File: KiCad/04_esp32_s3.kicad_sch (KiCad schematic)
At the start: 28 parts, among them IC101 ESP32-S3-WROOM-1-N16R8, Q300 SS8050, Q301 SS8050

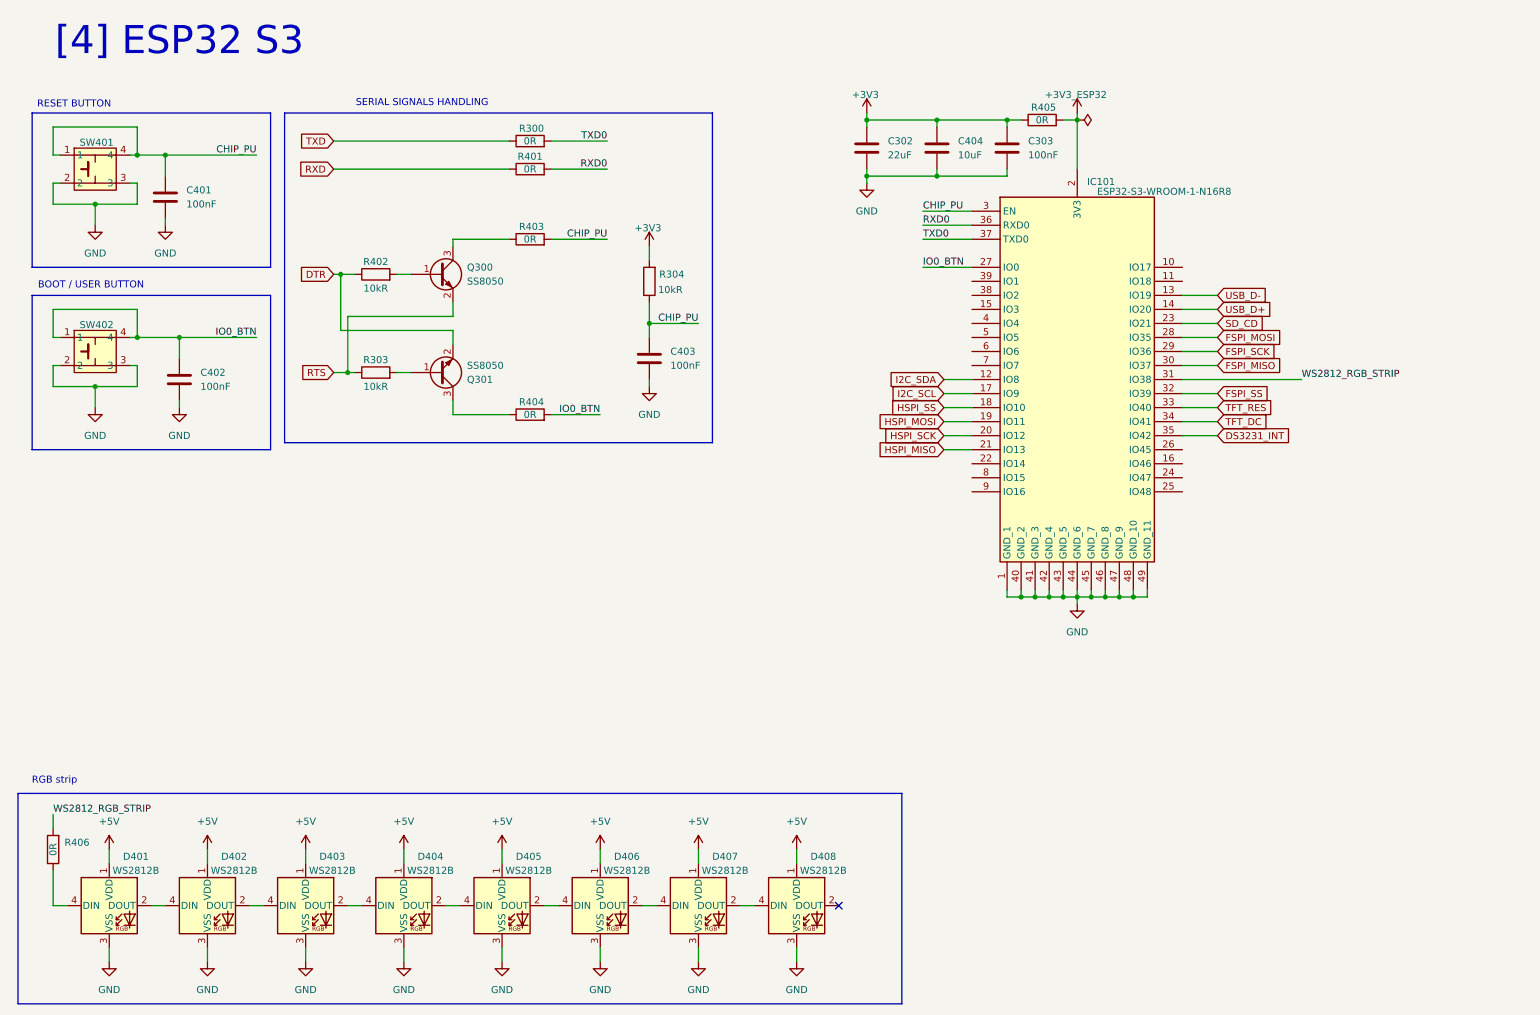
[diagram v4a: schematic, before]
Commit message: Add analog sensors
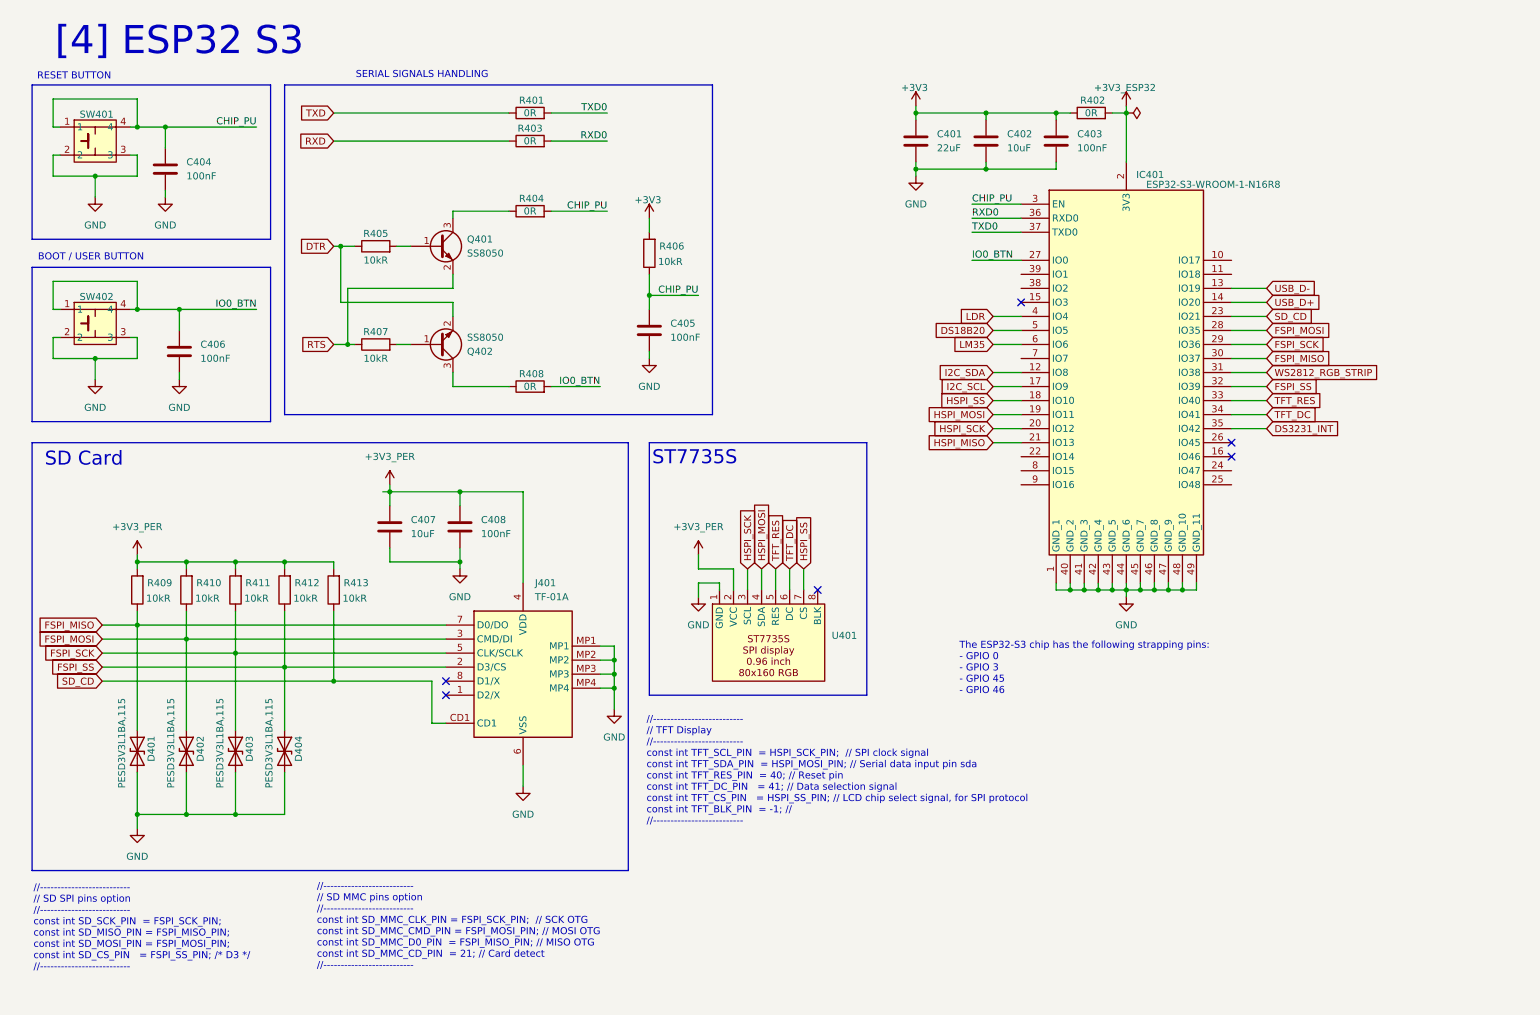
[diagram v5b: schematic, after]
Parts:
- removed D401, D402, D403, D404, D405, D406, D407, D408: WS2812B, LED_SMD:LED_WS2812B_PLCC4_5.0x5.0mm_P3.2mm, symbol LED:WS2812B
- removed R406: 0R, Resistor_SMD:R_0805_2012Metric, symbol Device:R
- added C407: 10uF, Capacitor_SMD:C_0603_1608Metric, symbol Device:C
- added C408: 100nF, Capacitor_SMD:C_0603_1608Metric, symbol Device:C
- added D401, D402, D403, D404: PESD3V3L1BA,115, Diode_SMD:D_SOD-323, symbol Device:D_TVS
- added J401: TF-01A, esp32_s3_weather_webserver:TF01A, symbol esp32_s3_weather_webserver:TF-01A
- added R409, R410, R411, R412, R413: 10kR, Resistor_SMD:R_0805_2012Metric, symbol Device:R
- added U401: ~, symbol esp32_s3_weather_webserver:ST7735S
- renumbered C302 to C401, C404 to C402, C303 to C403, C401 to C404, C403 to C405, C402 to C406, IC101 to IC401, Q300 to Q401, Q301 to Q402, R300 to R401, R405 to R402, R401 to R403, R403 to R404, R402 to R405, R304 to R406, R303 to R407, R404 to R408
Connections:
- net FSPI_MISO: now also D401.1 (A1), J401.7 (D0/DO), R409.1
- net FSPI_MOSI: now also D402.1 (A1), J401.3 (CMD/DI), R410.1
- net FSPI_SCK: now also D403.1 (A1), J401.5 (CLK/SCLK), R411.1
- net FSPI_SS: now also D404.1 (A1), J401.2 (D3/CS), R412.1
- net GND: now also C407.2, C408.2, D401.2 (A2), D402.2 (A2), D403.2 (A2), D404.2 (A2), J401.6 (VSS), J401.MP1, J401.MP2, J401.MP3, J401.MP4, U401.1 (GND)
- net HSPI_MOSI: now also U401.4 (SDA)
- net HSPI_SCK: now also U401.3 (SCL)
- net HSPI_SS: now also U401.7 (CS)
- net SD_CD: now also J401.CD1, R413.1
- net TFT_DC: now also U401.6 (DC)
- net TFT_RES: now also U401.5 (RES)
- net LDR: now reaches IC401.4 (IO4)
- net DS18B20: now reaches IC401.5 (IO5)
- net LM35: now reaches IC401.6 (IO6)
- new net +3V3_PER: C407.1, C408.1, J401.4 (VDD), R409.2, R410.2, R411.2, R412.2, R413.2, U401.2 (VCC)
- no-connect marks 1 -> 6
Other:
- note added: "//-------------------------- // SD MMC pins option //-------------------------- const int SD_MMC_CLK_PIN = FSPI_SCK_PIN; // SCK OTG const int SD_MMC_CMD_PIN = FSPI_MOSI_PIN; // MOSI OTG const int SD_MMC_D0_PIN = FSPI_MISO_PIN; // MISO OTG const int SD_MMC_CD_PIN = 21; // Card detect //--------------------------"
- note added: "//-------------------------- // SD SPI pins option //-------------------------- const int SD_SCK_PIN = FSPI_SCK_PIN; const int SD_MISO_PIN = FSPI_MISO_PIN; const int SD_MOSI_PIN = FSPI_MOSI_PIN; const int SD_CS_PIN = FSPI_SS_PIN; /* D3 */ //--------------------------"
- note added: "//-------------------------- // TFT Display //-------------------------- const int TFT_SCL_PIN = HSPI_SCK_PIN; // SPI clock signal const int TFT_SDA_PIN = HSPI_MOSI_PIN; // Serial data input pin sda const int TFT_RES_PIN = 40; // Reset pin const int TFT_DC_PIN = 41; // Data selection signal const int TFT_CS_PIN = HSPI_SS_PIN; // LCD chip select signal, for SPI protocol const int TFT_BLK_PIN = -1;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"
- note added: "SD Card"
- note added: "ST7735S"
- note added: "The ESP32-S3 chip has the following strapping pins: - GPIO 0 - GPIO 3 - GPIO 45 - GPIO 46"
- note removed: "RGB strip"
- moved on the sheet: C401, C402, C403, C404, C405, C406, IC401, Q401, Q402, R401, R402, R403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

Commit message: First scheme version
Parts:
- added C409: 100nF, Capacitor_SMD:C_0603_1608Metric, symbol Device:C
- added J401, J403: Conn_01x04_Pin, Connector_PinHeader_2.54mm:PinHeader_1x04_P2.54mm_Vertical, symbol Connector:Conn_01x04_Pin
- added J402: Conn_01x12_Pin, Connector_PinHeader_2.54mm:PinHeader_1x12_P2.54mm_Vertical, symbol Connector:Conn_01x12_Pin
- added R409: 10kR, Resistor_SMD:R_0805_2012Metric, symbol Device:R
- added SW403: ~, esp32_s3_weather_webserver:SW_PUSH_6mm_H5mm, symbol esp32_s3_weather_webserver:SW_PUSH_6mm_H5mm
- Q401, Q402: Manufacturer Jiangsu Changjing Electronics Technology Co., Ltd. -> (none); Manufacturer Part Number SS8050(RANGE:200-350) -> (none)
- renumbered J401 to J404, R402 to R401, R401 to R402, R406 to R404, R404 to R405, R405 to R406, R409 to R410, R410 to R411, R411 to R412, R412 to R413, R413 to R414
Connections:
- net +3V3: now also R409.1
- net +3V3_PER: now also J401.2 (Pin_2), J402.2 (Pin_2), J403.2 (Pin_2)
- net GND: now also C409.2, J401.1 (Pin_1), J402.10 (Pin_10), J402.4 (Pin_4), J402.6 (Pin_6), J403.1 (Pin_1), SW403.2, SW403.3
- net I2C_SCL: now also J403.4 (Pin_4)
- net I2C_SDA: now also J403.3 (Pin_3)
- net GPIO17: now reaches IC401.10 (IO17)
- net GPIO17: now also J402.8 (Pin_8)
- net GPIO18: now reaches IC401.11 (IO18)
- net GPIO18: now also J402.9 (Pin_9)
- net GPIO14: now reaches IC401.22 (IO14)
- net GPIO14: now also J402.7 (Pin_7)
- net GPIO47: now reaches IC401.24 (IO47)
- net GPIO47: now also J402.11 (Pin_11)
- net GPIO48: now reaches IC401.25 (IO48)
- net GPIO48: now also J402.12 (Pin_12)
- net GPIO2: now reaches IC401.38 (IO2)
- net GPIO2: now also J402.5 (Pin_5)
- net USR_BTN: now reaches IC401.39 (IO1)
- net USR_BTN: now also C409.1, R409.2, SW403.1, SW403.4
- net DHT11: now reaches IC401.7 (IO7)
- net RXD1: now reaches IC401.8 (IO15)
- net RXD1: now also J401.3 (Pin_3)
- net TXD1: now reaches IC401.9 (IO16)
- net TXD1: now also J401.4 (Pin_4)
- new net +3V3A: J402.3 (Pin_3)
- new net +5V: J402.1 (Pin_1)
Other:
- note added: "BOOT"
- note added: "External I2C Pin Header"
- note added: "External UART Pin Header"
- note added: "Spare Pins Header"
- note added: "User BUTTON"
- note removed: "BOOT / USER BUTTON"
- moved on the sheet: C401, C402, C403, C405, IC401, R401, R402, R403, R404, R405, R408

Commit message: Firmware refactoring. Beginning
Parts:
- removed C409: 100nF, Capacitor_SMD:C_0603_1608Metric, symbol Device:C
- removed J402: Conn_01x12_Pin, Connector_PinHeader_2.54mm:PinHeader_1x12_P2.54mm_Vertical, symbol Connector:Conn_01x12_Pin
- removed R409: 10kR, Resistor_SMD:R_0805_2012Metric, symbol Device:R
- removed SW403: ~, esp32_s3_weather_webserver:SW_PUSH_6mm_H5mm, symbol esp32_s3_weather_webserver:SW_PUSH_6mm_H5mm
- added J1: Conn_01x08_Pin, symbol Connector:Conn_01x08_Pin
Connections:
- net GPIO48 is gone; now on net WS2812_RGB_STRIP: IC401.25 (IO48)
- net +3V3A: now also J1.3 (Pin_3)
- net +3V3_PER: now also J1.2 (Pin_2)
- net +5V: now also J1.1 (Pin_1)
- net GND: now also J1.4 (Pin_4), J1.8 (Pin_8)
- net GPIO14: now also J1.6 (Pin_6)
- net GPIO2: now also J1.5 (Pin_5)
- net GPIO47: now also J1.7 (Pin_7)
- net WS2812_RGB_STRIP: no longer IC401.31 (IO38)
- net GPIO17 renamed USR_BTN_LEFT
- net GPIO18 renamed USR_BTN_RIGHT
- new net ONBOARD_LED: IC401.31 (IO38)
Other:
- note removed: "User BUTTON"

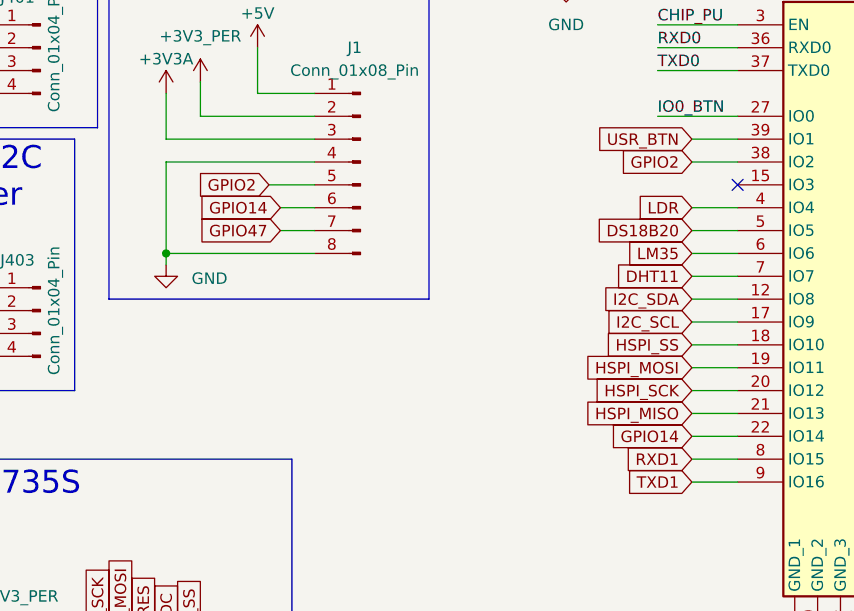
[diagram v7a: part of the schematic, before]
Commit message: Update BME280 Scheme, Add more sensors to firmware
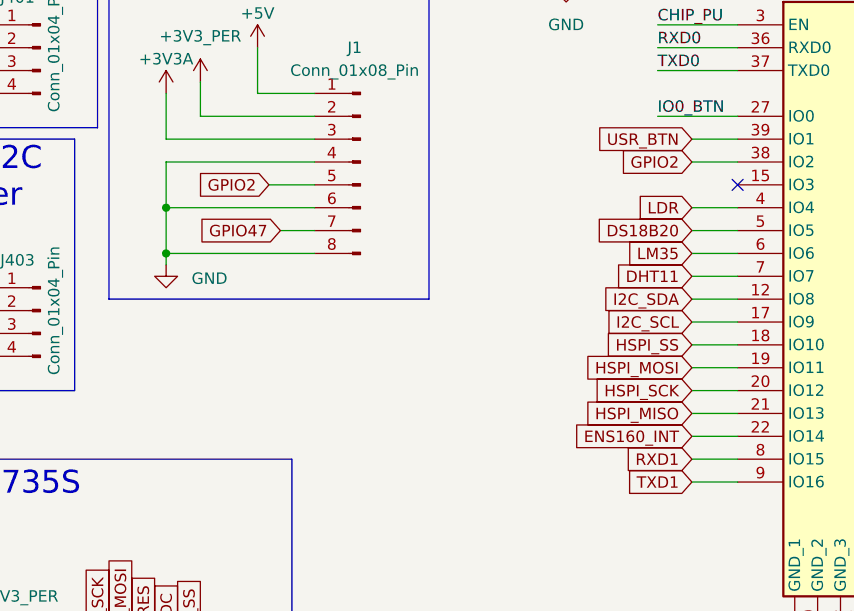
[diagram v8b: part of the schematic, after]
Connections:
- net GND: now also J1.6 (Pin_6)
- net GPIO14 renamed ENS160_INT
- net ENS160_INT: no longer J1.6 (Pin_6)
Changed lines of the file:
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@@
+	)
+	(junction
+		(at 153.67 66.04)
+		(diameter 0)
+		(color 0 0 0 0)
 	)
 	(junction
@@
 	(wire
 		(pts
-			(xy 153.67 60.96) (xy 153.67 71.12)
+			(xy 153.67 60.96) (xy 153.67 66.04)
 		)
 		(stroke
@@
 	(wire
 		(pts
-			(xy 166.37 66.04) (xy 170.18 66.04)
-		)
-		(stroke
-			(width 0)
-			(type default)
-		)
-	)
-	(wire
-		(pts
 			(xy 62.23 161.29) (xy 53.34 161.29)
 		)
@@
 	(wire
 		(pts
+			(xy 153.67 66.04) (xy 153.67 71.12)
+		)
+		(stroke
+			(width 0)
+			(type default)
+		)
+	)
+	(wire
+		(pts
 			(xy 40.64 36.83) (xy 57.15 36.83)
 		)
@@
 		(pts
 			(xy 208.28 55.88) (xy 217.17 55.88)
+		)
+		(stroke
+			(width 0)
+			(type default)
+		)
+	)
+	(wire
+		(pts
+			(xy 153.67 66.04) (xy 170.18 66.04)
 		)
 		(stroke
@@
 		)
 	)
+	(global_label "ENS160_INT"
+		(shape input)
+		(at 212.09 91.44 180)
+		(fields_autoplaced yes)
+		(effects
+			(font
+				(size 1.27 1.27)
+			)
+			(justify right)
+		)
+		(property "Intersheetrefs" "${INTERSHEET_REFS}"
+			(at 197.9168 91.44 0)
+			(effects
+				(font
+					(size 1.27 1.27)
+				)
+				(justify right)
+				(hide yes)
+			)
+		)
+	)
 	(global_label "DTR"
 		(shape input)
@@
 		)
 	)
-	(global_label "GPIO14"
-		(shape input)
-		(at 212.09 91.44 180)
+	(global_label "USB_D-"
+		(shape input)
+		(at 261.62 60.96 0)
+		(fields_autoplaced yes)
+		(effects
+			(font
+				(size 1.27 1.27)
+			)
+			(justify left)
+		)
+		(property "Intersheetrefs" "${INTERSHEET_REFS}"
+			(at 272.2252 60.96 0)
+			(effects
+				(font
+					(size 1.27 1.27)
+				)
+				(justify left)
+				(hide yes)
+			)
+		)
+	)
+	(global_label "I2C_SDA"
+		(shape input)
+		(at 212.09 76.2 180)
+		(fields_autoplaced yes)
+		(effects
+			(font
+				(size 1.27 1.27)
+			)
+			(justify right)
+		)
+		(property "Intersheetrefs" "${INTERSHEET_REFS}"
+			(at 201.4848 76.2 0)
+			(effects
+				(font
+					(size 1.27 1.27)
+				)
+				(justify right)
+				(hide yes)
+			)
+		)
+	)
+	(global_label "GPIO47"
+		(shape input)
+		(at 261.62 93.98 0)
 		(fields_autoplaced yes)
 		(effects
@@
 				(color 7 10 255 1)
 			)
+			(justify left)
+		)
+		(property "Intersheetrefs" "${INTERSHEET_REFS}"
+			(at 271.4995 93.98 0)
+			(effects
+				(font
+					(size 1.27 1.27)
+				)
+				(justify left)
+				(hide yes)
+			)
+		)
+	)
+	(global_label "HSPI_MOSI"
+		(shape input)
+		(at 212.09 83.82 180)
+		(fields_autoplaced yes)
+		(effects
+			(font
+				(size 1.27 1.27)
+			)
 			(justify right)
 		)
 		(property "Intersheetrefs" "${INTERSHEET_REFS}"
-			(at 202.2105 91.44 0)
+			(at 199.1262 83.82 0)
 			(effects
 				(font
@@
 		)
 	)
-	(global_label "USB_D-"
-		(shape input)
-		(at 261.62 60.96 0)
+	(global_label "HSPI_MOSI"
+		(shape input)
+		(at 148.59 116.84 90)
 		(fields_autoplaced yes)
 		(effects
@@
 		)
 		(property "Intersheetrefs" "${INTERSHEET_REFS}"
-			(at 272.2252 60.96 0)
+			(at 148.59 103.8762 90)
 			(effects
 				(font
@@
 		)
 	)
-	(global_label "I2C_SDA"
-		(shape input)
-		(at 212.09 76.2 180)
+	(global_label "RTS"
+		(shape input)
+		(at 71.12 76.2 180)
 		(fields_autoplaced yes)
 		(effects
@@
 		)
 		(property "Intersheetrefs" "${INTERSHEET_REFS}"
-			(at 201.4848 76.2 0)
+			(at 64.6877 76.2 0)
 			(effects
 				(font
@@
 		)
 	)
+	(global_label "SD_CD"
+		(shape input)
+		(at 261.62 66.04 0)
+		(fields_autoplaced yes)
+		(effects
+			(font
+				(size 1.27 1.27)
+			)
+			(justify left)
+		)
+		(property "Intersheetrefs" "${INTERSHEET_REFS}"
+			(at 270.5923 66.04 0)
+			(effects
+				(font
+					(size 1.27 1.27)
+				)
+				(justify left)
+				(hide yes)
+			)
+		)
+	)
 	(global_label "GPIO47"
 		(shape input)
-		(at 261.62 93.98 0)
+		(at 166.37 68.58 180)
 		(fields_autoplaced yes)
 		(effects
@@
 				(color 7 10 255 1)
 			)
+			(justify right)
+		)
+		(property "Intersheetrefs" "${INTERSHEET_REFS}"
+			(at 156.4905 68.58 0)
+			(effects
+				(font
+					(size 1.27 1.27)
+				)
+				(justify right)
+				(hide yes)
+			)
+		)
+	)
+	(global_label "TFT_DC"
+		(shape input)
+		(at 153.67 116.84 90)
+		(fields_autoplaced yes)
+		(effects
+			(font
+				(size 1.27 1.27)
+			)
 			(justify left)
 		)
 		(property "Intersheetrefs" "${INTERSHEET_REFS}"
-			(at 271.4995 93.98 0)
+			(at 153.67 107.3234 90)
 			(effects
 				(font
@@
 		)
 	)
-	(global_label "HSPI_MOSI"
-		(shape input)
-		(at 212.09 83.82 180)
+	(global_label "TXD1"
+		(shape input)
+		(at 212.09 96.52 180)
 		(fields_autoplaced yes)
 		(effects
@@
 		)
 		(property "Intersheetrefs" "${INTERSHEET_REFS}"
-			(at 199.1262 83.82 0)
+			(at 204.4482 96.52 0)
 			(effects
 				(font
@@
 		)
 	)
-	(global_label "HSPI_MOSI"
-		(shape input)
-		(at 148.59 116.84 90)
-		(fields_autoplaced yes)
-		(effects
-			(font
-				(size 1.27 1.27)
-			)
-			(justify left)
-		)
-		(property "Intersheetrefs" "${INTERSHEET_REFS}"
-			(at 148.59 103.8762 90)
-			(effects
-				(font
-					(size 1.27 1.27)
-				)
-				(justify left)
-				(hide yes)
-			)
-		)
-	)
-	(global_label "RTS"
-		(shape input)
-		(at 71.12 76.2 180)
+	(global_label "DHT11"
+		(shape input)
+		(at 212.09 73.66 180)
 		(fields_autoplaced yes)
 		(effects
@@
 		)
 		(property "Intersheetrefs" "${INTERSHEET_REFS}"
-			(at 64.6877 76.2 0)
+			(at 203.1177 73.66 0)
 			(effects
 				(font
@@
 		)
 	)
-	(global_label "SD_CD"
-		(shape input)
-		(at 261.62 66.04 0)
-		(fields_autoplaced yes)
-		(effects
-			(font
-				(size 1.27 1.27)
-			)
-			(justify left)
-		)
-		(property "Intersheetrefs" "${INTERSHEET_REFS}"
-			(at 270.5923 66.04 0)
-			(effects
-				(font
-					(size 1.27 1.27)
-				)
-				(justify left)
-				(hide yes)
-			)
-		)
-	)
-	(global_label "GPIO47"
-		(shape input)
-		(at 166.37 68.58 180)
-		(fields_autoplaced yes)
-		(effects
-			(font
-				(size 1.27 1.27)
-				(color 7 10 255 1)
+	(global_label "LM35"
+		(shape input)
+		(at 212.09 71.12 180)
+		(fields_autoplaced yes)
+		(effects
+			(font
+				(size 1.27 1.27)
 			)
 			(justify right)
 		)
 		(property "Intersheetrefs" "${INTERSHEET_REFS}"
-			(at 156.4905 68.58 0)
-			(effects
-				(font
-					(size 1.27 1.27)
-				)
-				(justify right)
-				(hide yes)
-			)
-		)
-	)
-	(global_label "TFT_DC"
-		(shape input)
-		(at 153.67 116.84 90)
-		(fields_autoplaced yes)
-		(effects
-			(font
-				(size 1.27 1.27)
-			)
-			(justify left)
-		)
-		(property "Intersheetrefs" "${INTERSHEET_REFS}"
-			(at 153.67 107.3234 90)
-			(effects
-				(font
-					(size 1.27 1.27)
-				)
-				(justify left)
-				(hide yes)
-			)
-		)
-	)
-	(global_label "TXD1"
-		(shape input)
-		(at 212.09 96.52 180)
-		(fields_autoplaced yes)
-		(effects
-			(font
-				(size 1.27 1.27)
-			)
-			(justify right)
-		)
-		(property "Intersheetrefs" "${INTERSHEET_REFS}"
-			(at 204.4482 96.52 0)
-			(effects
-				(font
-					(size 1.27 1.27)
-				)
-				(justify right)
-				(hide yes)
-			)
-		)
-	)
-	(global_label "DHT11"
-		(shape input)
-		(at 212.09 73.66 180)
-		(fields_autoplaced yes)
-		(effects
-			(font
-				(size 1.27 1.27)
-			)
-			(justify right)
-		)
-		(property "Intersheetrefs" "${INTERSHEET_REFS}"
-			(at 203.1177 73.66 0)
-			(effects
-				(font
-					(size 1.27 1.27)
-				)
-				(justify right)
-				(hide yes)
-			)
-		)
-	)
-	(global_label "LM35"
-		(shape input)
-		(at 212.09 71.12 180)
-		(fields_autoplaced yes)
-		(effects
-			(font
-				(size 1.27 1.27)
-			)
-			(justify right)
-		)
-		(property "Intersheetrefs" "${INTERSHEET_REFS}"
 			(at 204.2063 71.12 0)
 			(effects
 				(font
-					(size 1.27 1.27)
-				)
-				(justify right)
-				(hide yes)
-			)
-		)
-	)
-	(global_label "GPIO14"
-		(shape input)
-		(at 166.37 66.04 180)
-		(fields_autoplaced yes)
-		(effects
-			(font
-				(size 1.27 1.27)
-				(color 7 10 255 1)
-			)
-			(justify right)
-		)
-		(property "Intersheetrefs" "${INTERSHEET_REFS}"
-			(at 156.4905 66.04 0)
-			(effects
-				(font
